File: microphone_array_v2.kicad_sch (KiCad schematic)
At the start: 134 parts, among them J1 RPi_P1_26, J2 Tang_Nano_9K, J3 Tang_Nano_9K, U1 LP5907MFX-3.3, U2 SN74LVC244A, U3 USBLC6-4SC6, U4 USBLC6-4SC6, X1 24.576MHz

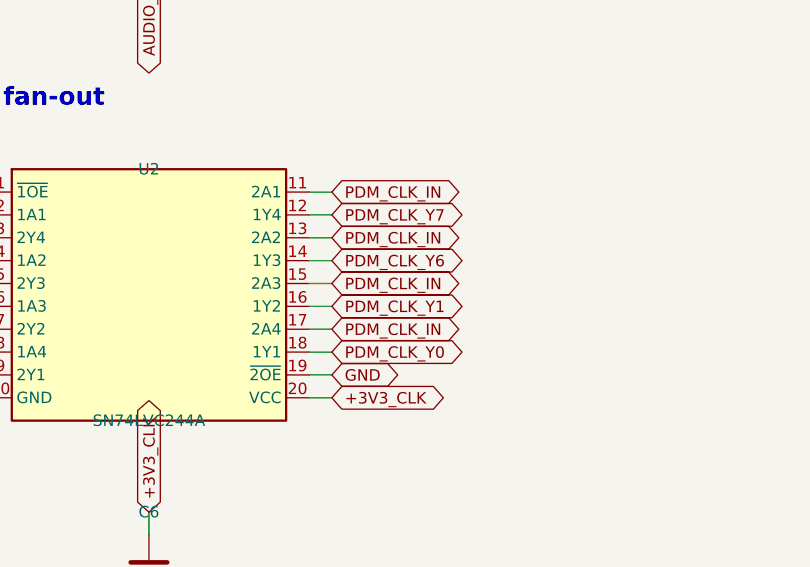
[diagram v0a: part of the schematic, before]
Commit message: Asked Claude to remove routes that hit each other, then it ran out of tokens
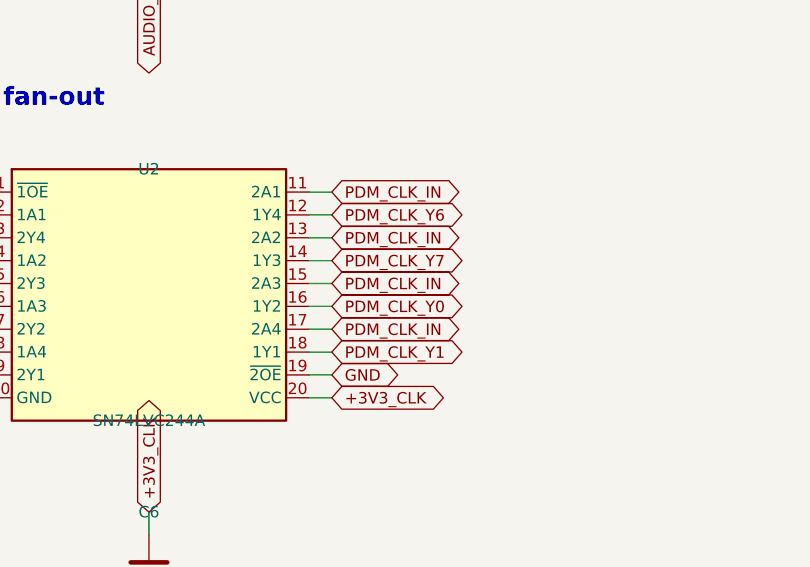
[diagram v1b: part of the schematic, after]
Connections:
- net PDM_CLK_Y0: now also U2.16 (1Y2); no longer U2.18 (1Y1)
- net PDM_CLK_Y1: now also U2.18 (1Y1); no longer U2.16 (1Y2)
- net PDM_CLK_Y6: now also U2.12 (1Y4); no longer U2.14 (1Y3)
- net PDM_CLK_Y7: now also U2.14 (1Y3); no longer U2.12 (1Y4)
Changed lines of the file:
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@@
 		)
 	)
-	(global_label "PDM_CLK_Y7"
+	(global_label "PDM_CLK_Y6"
 		(shape bidirectional)
 		(at 297.18 217.17 0)
@@
 		)
 	)
-	(global_label "PDM_CLK_Y6"
+	(global_label "PDM_CLK_Y7"
 		(shape bidirectional)
 		(at 297.18 222.25 0)
@@
 		)
 	)
-	(global_label "PDM_CLK_Y1"
+	(global_label "PDM_CLK_Y0"
 		(shape bidirectional)
 		(at 297.18 227.33 0)
@@
 		)
 	)
-	(global_label "PDM_CLK_Y0"
+	(global_label "PDM_CLK_Y1"
 		(shape bidirectional)
 		(at 297.18 232.41 0)

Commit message: Claude fixup
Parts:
- removed TP1: +5V, TestPoint:TestPoint_Pad_D1.5mm, symbol Connector:TestPoint
- removed TP10: SPI_MOSI, TestPoint:TestPoint_Pad_D1.5mm, symbol Connector:TestPoint
- removed TP11: SPI_MISO, TestPoint:TestPoint_Pad_D1.5mm, symbol Connector:TestPoint
- removed TP12: SPI_CS_N, TestPoint:TestPoint_Pad_D1.5mm, symbol Connector:TestPoint
- removed TP13: PDM_D0, TestPoint:TestPoint_Pad_D1.5mm, symbol Connector:TestPoint
- removed TP14: PDM_D1, TestPoint:TestPoint_Pad_D1.5mm, symbol Connector:TestPoint
- removed TP15: PDM_D2, TestPoint:TestPoint_Pad_D1.5mm, symbol Connector:TestPoint
- removed TP16: PDM_D3, TestPoint:TestPoint_Pad_D1.5mm, symbol Connector:TestPoint
- removed TP17: PDM_D4, TestPoint:TestPoint_Pad_D1.5mm, symbol Connector:TestPoint
- removed TP18: PDM_D5, TestPoint:TestPoint_Pad_D1.5mm, symbol Connector:TestPoint
- removed TP19: PDM_D6, TestPoint:TestPoint_Pad_D1.5mm, symbol Connector:TestPoint
- removed TP2: +3V3A, TestPoint:TestPoint_Pad_D1.5mm, symbol Connector:TestPoint
- removed TP20: PDM_D7, TestPoint:TestPoint_Pad_D1.5mm, symbol Connector:TestPoint
- removed TP21: HOST_IRQ, TestPoint:TestPoint_Pad_D1.5mm, symbol Connector:TestPoint
- removed TP22: HOST_SYNC, TestPoint:TestPoint_Pad_D1.5mm, symbol Connector:TestPoint
- removed TP23: HOST_RESET_N, TestPoint:TestPoint_Pad_D1.5mm, symbol Connector:TestPoint
- removed TP24: HOST_STATUS, TestPoint:TestPoint_Pad_D1.5mm, symbol Connector:TestPoint
- removed TP3: +3V3_CLK, TestPoint:TestPoint_Pad_D1.5mm, symbol Connector:TestPoint
- removed TP4: TANG_3V3, TestPoint:TestPoint_Pad_D1.5mm, symbol Connector:TestPoint
- removed TP5, TP8: GND, TestPoint:TestPoint_Pad_D1.5mm, symbol Connector:TestPoint
- removed TP6: AUDIO_MCLK, TestPoint:TestPoint_Pad_D1.5mm, symbol Connector:TestPoint
- removed TP7: PDM_CLK_IN, TestPoint:TestPoint_Pad_D1.5mm, symbol Connector:TestPoint
- removed TP9: SPI_SCLK, TestPoint:TestPoint_Pad_D1.5mm, symbol Connector:TestPoint
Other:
- note removed: "Test points TP1-TP8"
- note removed: "Test points TP17-TP24"
- note removed: "Test points TP9-TP16"

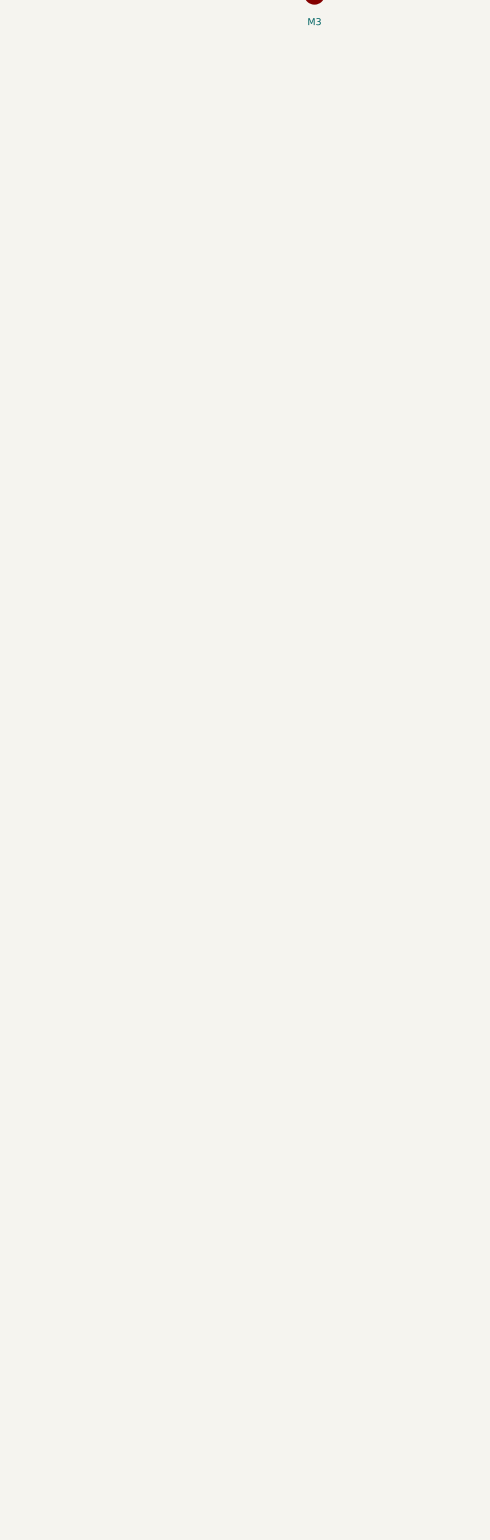
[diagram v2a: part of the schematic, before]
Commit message: Placed test points, generated release
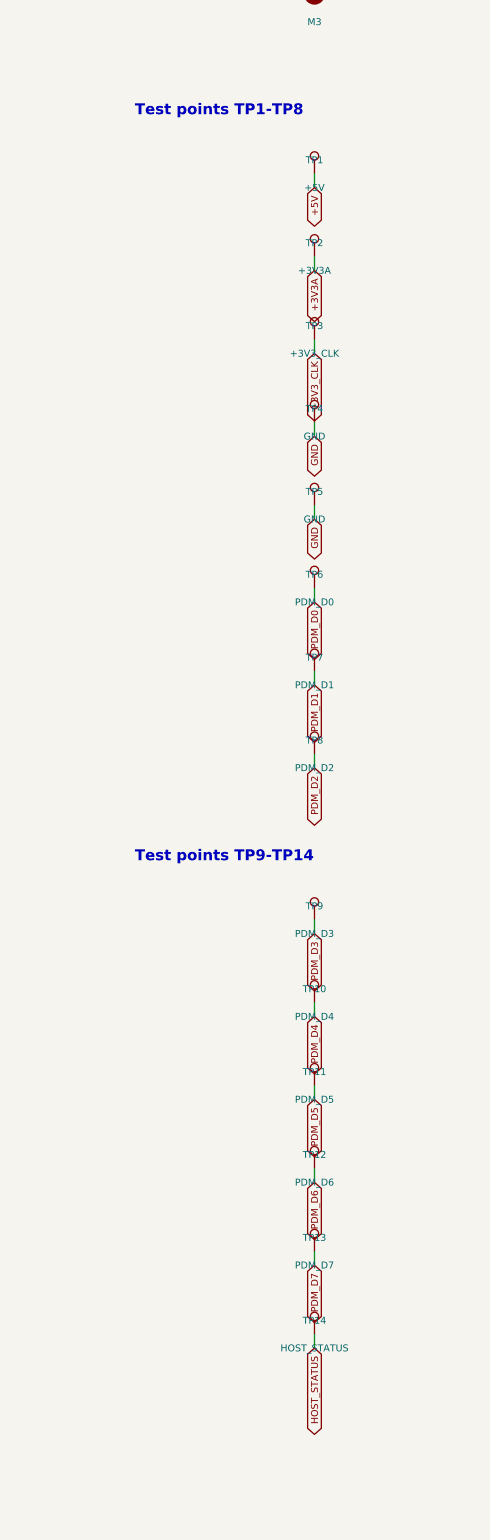
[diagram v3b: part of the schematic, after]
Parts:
- added TP1: +5V, MicArrayV2:TestPoint_Pad_D1.0mm_NoSilk, symbol Connector:TestPoint
- added TP10: PDM_D4, MicArrayV2:TestPoint_Pad_D1.5mm_NoSilk, symbol Connector:TestPoint
- added TP11: PDM_D5, MicArrayV2:TestPoint_Pad_D1.5mm_NoSilk, symbol Connector:TestPoint
- added TP12: PDM_D6, MicArrayV2:TestPoint_Pad_D1.5mm_NoSilk, symbol Connector:TestPoint
- added TP13: PDM_D7, MicArrayV2:TestPoint_Pad_D1.5mm_NoSilk, symbol Connector:TestPoint
- added TP14: HOST_STATUS, MicArrayV2:TestPoint_Pad_D1.0mm_NoSilk, symbol Connector:TestPoint
- added TP2: +3V3A, MicArrayV2:TestPoint_Pad_D1.5mm_NoSilk, symbol Connector:TestPoint
- added TP3: +3V3_CLK, MicArrayV2:TestPoint_Pad_D1.5mm_NoSilk, symbol Connector:TestPoint
- added TP4, TP5: GND, MicArrayV2:TestPoint_Pad_D1.5mm_NoSilk, symbol Connector:TestPoint
- added TP6: PDM_D0, MicArrayV2:TestPoint_Pad_D1.5mm_NoSilk, symbol Connector:TestPoint
- added TP7: PDM_D1, MicArrayV2:TestPoint_Pad_D1.5mm_NoSilk, symbol Connector:TestPoint
- added TP8: PDM_D2, MicArrayV2:TestPoint_Pad_D1.5mm_NoSilk, symbol Connector:TestPoint
- added TP9: PDM_D3, MicArrayV2:TestPoint_Pad_D1.5mm_NoSilk, symbol Connector:TestPoint
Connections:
- net +3V3A: now also TP2.1
- net +3V3_CLK: now also TP3.1
- net +5V: now also TP1.1
- net GND: now also TP4.1, TP5.1
- net HOST_STATUS: now also TP14.1
- net PDM_D0: now also TP6.1
- net PDM_D1: now also TP7.1
- net PDM_D2: now also TP8.1
- net PDM_D3: now also TP9.1
- net PDM_D4: now also TP10.1
- net PDM_D5: now also TP11.1
- net PDM_D6: now also TP12.1
- net PDM_D7: now also TP13.1
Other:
- note added: "Test points TP1-TP8"
- note added: "Test points TP9-TP14"

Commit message: New board rev
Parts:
- removed H1, H2, H3, H4: M3, MountingHole:MountingHole_3.2mm_M3, symbol Mechanical:MountingHole
- J1: footprint Connector_PinHeader_2.54mm:PinHeader_2x13_P2.54mm_Vertical -> Connector_PinSocket_2.54mm:PinSocket_2x13_P2.54mm_Vertical
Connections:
- net PI_CS_N: now also U3.6 (IO4); no longer U3.4 (IO3)
- net PI_IRQ: now also U4.3 (IO2); no longer U4.1 (IO1)
- net PI_MISO: now also U3.4 (IO3); no longer U3.6 (IO4)
- net PI_MOSI: now also U4.1 (IO1); no longer U4.3 (IO2)
- net PI_RESET_N: now also U3.3 (IO2); no longer U3.1 (IO1)
- net PI_SCLK: now also U3.1 (IO1); no longer U3.3 (IO2)
- net PI_STATUS: now also U4.6 (IO4); no longer U4.4 (IO3)
- net PI_SYNC: now also U4.4 (IO3); no longer U4.6 (IO4)
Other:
- note removed: "Mounting holes"
- moved on the sheet: TP1, TP10, TP11, TP12, TP13, TP14, TP2, TP3, TP4, TP5, TP6, TP7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
